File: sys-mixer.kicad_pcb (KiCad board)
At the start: 2 copper layers, 122 x 84 mm, 16 parts, among them J1 RCA L&R, J2 RCA L&R, J3 RCA L&R, SW1 4PDT

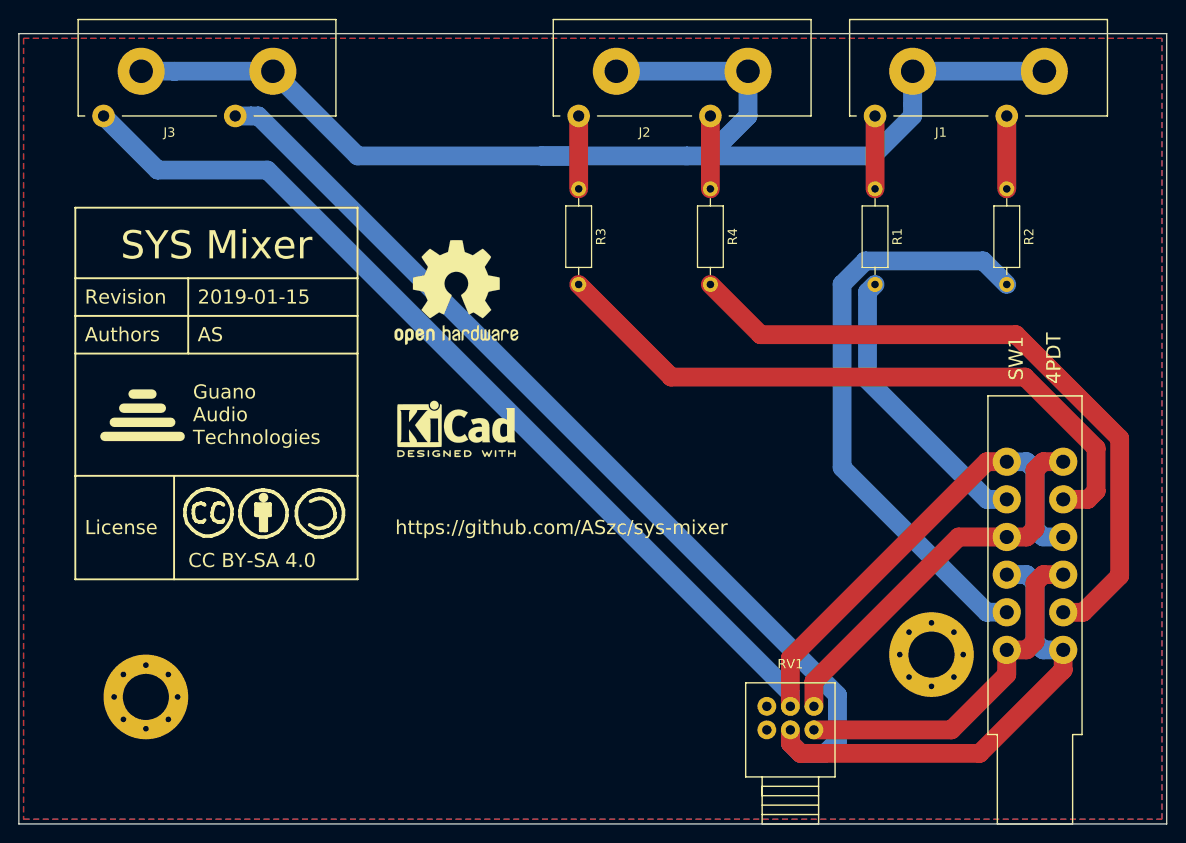
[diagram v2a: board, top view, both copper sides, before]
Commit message: Fix resistor position in schematic
Having the resistors right after the inputs causes the mixing to
misbehave.

Also tweaked mounting hole and control positions, based on fitting of
2019-01-15 boards.
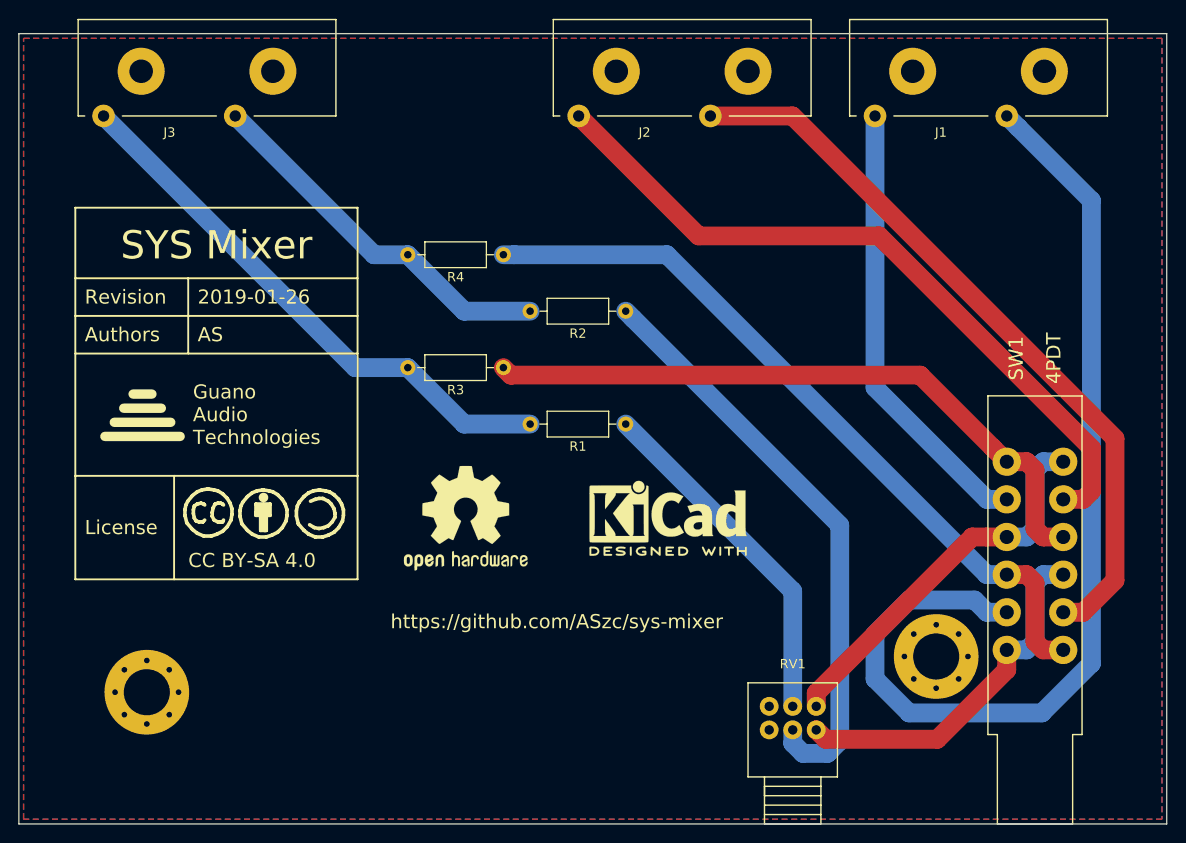
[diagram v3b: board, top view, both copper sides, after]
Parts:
- removed the REF** at (96.5, 67.0)
- added REF**: KiCad-Logo2_8mm_SilkScreen, Symbol:KiCad-Logo2_8mm_SilkScreen, F.Cu at (119.0, 76.5)
- moved R2 42.5 mm to (114.5, 54.5), turned to 180 degrees
- moved R1 36.4 mm to (114.5, 66.5), turned to 180 degrees
- moved REF** 24.0 mm to (97.5, 76.5)
- moved R4 23.1 mm to (101.5, 48.5), turned to 180 degrees
- moved R3 20.6 mm to (101.5, 60.5), turned to 180 degrees
- moved H2 0.54 mm to (147.5, 91.2)
- moved H1 0.51 mm to (63.6, 95.0)
- moved RV1 0.25 mm to (132.2, 109.0)
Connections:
- R1 pad 1: Net-(J1-Pad1) -> Net-(R1-Pad1)
- R1 pad 2: Net-(R1-Pad2) -> Net-(J3-Pad1)
- R2 pad 1: Net-(J1-Pad2) -> Net-(R2-Pad1)
- R2 pad 2: Net-(R2-Pad2) -> Net-(J3-Pad2)
- R3 pad 1: Net-(J2-Pad1) -> Net-(R3-Pad1)
- R3 pad 2: Net-(R3-Pad2) -> Net-(J3-Pad1)
- R4 pad 1: Net-(J2-Pad2) -> Net-(R4-Pad1)
- R4 pad 2: Net-(R4-Pad2) -> Net-(J3-Pad2)
- RV1 pad 2: Net-(J3-Pad2) -> Net-(R2-Pad1)
- RV1 pad 5: Net-(J3-Pad1) -> Net-(R1-Pad1)
- SW1 pad 10: Net-(J3-Pad1) -> Net-(R3-Pad1)
- SW1 pad 12: Net-(R3-Pad2) -> Net-(J2-Pad1)
- SW1 pad 2: Net-(J3-Pad2) -> Net-(R4-Pad1)
- SW1 pad 3: Net-(R2-Pad2) -> Net-(J1-Pad2)
- SW1 pad 5: Net-(J3-Pad1) -> Net-(R3-Pad1)
- SW1 pad 6: Net-(R1-Pad2) -> Net-(J1-Pad1)
- SW1 pad 7: Net-(J3-Pad2) -> Net-(R4-Pad1)
- SW1 pad 9: Net-(R4-Pad2) -> Net-(J2-Pad2)
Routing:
- net Net-(H1-Pad1): track 134.7 -> 0.00 mm
- net Net-(J3-Pad2): track 151.9 -> 39.9 mm
- net Net-(J1-Pad2): track 7.75 -> 109.4 mm
- net Net-(J3-Pad1): track 149.6 -> 58.9 mm
- net Net-(R4-Pad1): track 0.00 -> 81.1 mm
- net Net-(R4-Pad2): track 72.9 -> 0.00 mm
- net Net-(J2-Pad2): track 7.75 -> 79.6 mm
- net Net-(R3-Pad2): track 71.1 -> 0.00 mm
- net Net-(R3-Pad1): track 0.00 -> 70.6 mm
- net Net-(J2-Pad1): track 7.75 -> 77.5 mm
- net Net-(R2-Pad2): track 62.9 -> 0.00 mm
- net Net-(R2-Pad1): track 0.00 -> 62.5 mm
- net Net-(J1-Pad1): track 7.75 -> 47.8 mm
- net Net-(R1-Pad1): track 0.00 -> 37.4 mm
- net Net-(R1-Pad2): track 30.5 -> 0.00 mm
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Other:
- board text added: "2019-01-26"
- board text removed: "2019-01-15"
